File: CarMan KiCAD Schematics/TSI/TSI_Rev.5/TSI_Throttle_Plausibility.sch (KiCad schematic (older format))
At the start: 69 parts, among them Q2 MMBF170, SW1 TS5A3159DBVT, U16 TS372CDT, U18 MCP6004, U22 MCP23016-I_SO, U23 DAC5574IDGS, U3 TS912, U30 TLP293, U6 TS912, U7 MCP6004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

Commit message: Datasheets and notes
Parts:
- SW1: Details (none) -> Analog Switch
- U16: MPN TS372CDT -> (none); OC_FARNELL 1094371 -> (none); PACKAGE 8-SOIC -> (none)
- U22: Field4 Unavailable -> (none); Field5 Microchip -> (none); Field8 None -> (none)
- U23: Details (none) -> 8-bit, Quad, Digital-to-Analog Converter with I2C interface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; Field4 8-bit, Quad, Digital-to-Analog Converter with I2C interface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 -> (none); Field5 None -> (none); Field6 DAC5574IDGS -> (none); Field7 Unavailable -> (none); Field8 Texas Instruments -> (none); Man. (none) -> Texas Instruments
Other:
- note added: "TP \n(J16)"
- note removed: "TP\n(J16)"
- moved on the sheet: C10, C27, C3, C7, D11, D2, D4, R1, R103, R17, R18, R19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

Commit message: General numbering
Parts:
- renumbered RV4 to RV2
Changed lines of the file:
@@
 	5900 2900 5900 2800
 $Comp
-L Device:R_POT_TRIM RV4
+L Device:R_POT_TRIM RV2
 U 1 1 60292796
 P 5900 2200
-F 0 "RV4" H 5830 2246 50  0000 R CNN
+F 0 "RV2" H 5830 2246 50  0000 R CNN
 F 1 "1K" H 5830 2155 50  0000 R CNN
 F 2 "TSI_Rev_2021_Footprint_Lib:Potentiometer" H 5900 2200 50  0001 C CNN

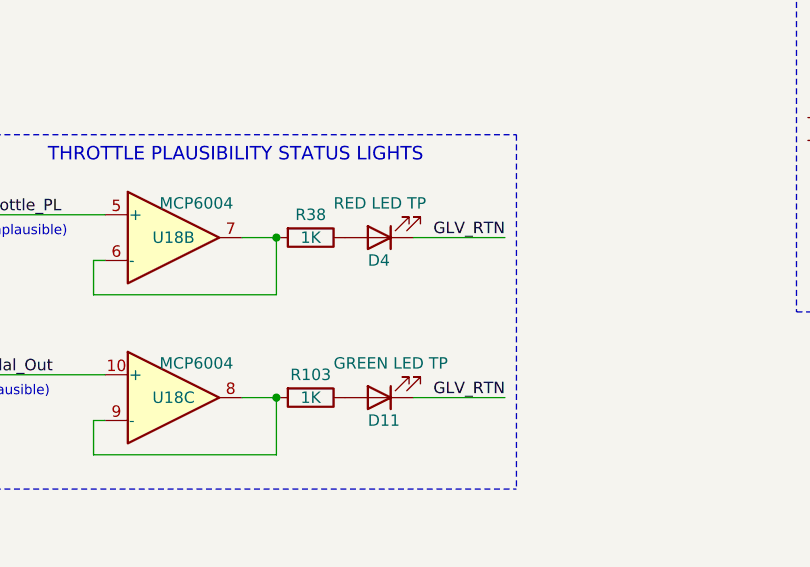
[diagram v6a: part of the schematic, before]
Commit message: Added jumpers across HV-, HV+ & MC+ voltage dividers Comments added to PC Circuit
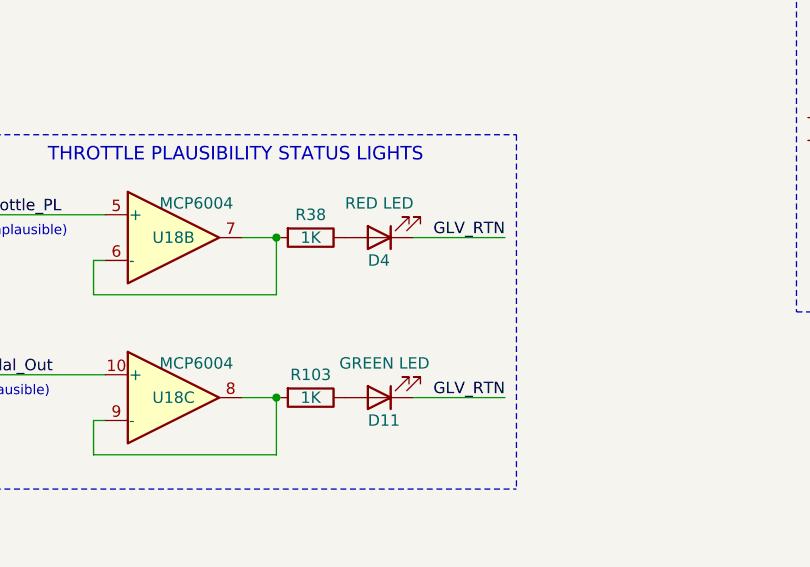
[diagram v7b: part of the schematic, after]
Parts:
- D11: value GREEN LED TP -> GREEN LED
- D4: value RED LED TP -> RED LED
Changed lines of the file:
@@
 AR Path="/5FC85F57/60834B36" Ref="D4"  Part="1"
 F 0 "D4" H 10175 9675 50  0000 R CNN
-F 1 "RED LED TP" H 10325 9425 50  0000 R CNN
+F 1 "RED LED" H 10275 9425 50  0000 R CNN
 F 2 "LED_SMD:LED_0805_2012Metric_Pad1.15x1.40mm_HandSolder" H 10125 9575 50  0001 C CNN
 F 3 "https://www.mouser.com/datasheet/2/678/av02-0112en-ds-hsmx-c1xx-29sep2010-1827222.pdf" H 10125 9575 50  0001 C CNN
@@
 AR Path="/5FC85F57/60823F7C" Ref="D11"  Part="1"
 F 0 "D11" H 10175 10375 50  0000 R CNN
-F 1 "GREEN LED TP" H 10325 10125 50  0000 R CNN
+F 1 "GREEN LED" H 10300 10125 50  0000 R CNN
 F 2 "LED_SMD:LED_0805_2012Metric_Pad1.15x1.40mm_HandSolder" H 10125 10275 50  0001 C CNN
 F 3 "https://www.mouser.com/datasheet/2/678/av02-0112en-ds-hsmx-c1xx-29sep2010-1827222.pdf" H 10125 10275 50  0001 C CNN

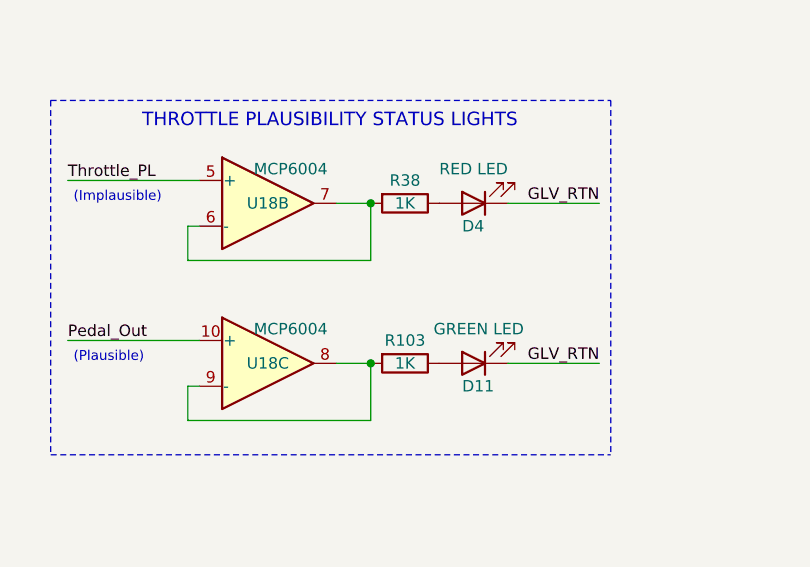
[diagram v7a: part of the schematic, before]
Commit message: Updated Resistor values for LEDs
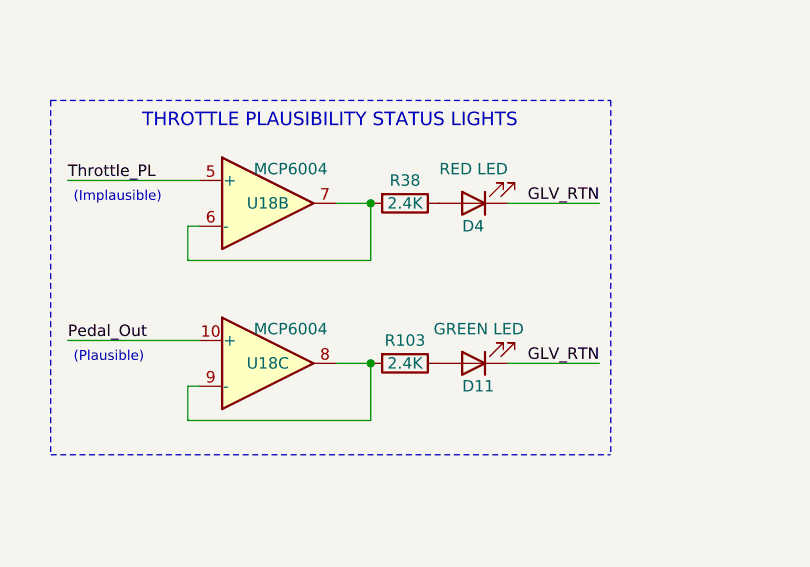
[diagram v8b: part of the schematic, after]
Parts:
- R103, R38: value 1K -> 2.4K
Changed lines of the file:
@@
 P 9825 9575
 F 0 "R38" V 9725 9575 50  0000 C CNN
-F 1 "1K" V 9825 9575 50  0000 C CNN
+F 1 "2.4K" V 9825 9575 50  0000 C CNN
 F 2 "Resistor_SMD:R_0805_2012Metric_Pad1.15x1.40mm_HandSolder" V 9755 9575 50  0001 C CNN
 F 3 "~" H 9825 9575 50  0001 C CNN
@@
 P 9825 10275
 F 0 "R103" V 9725 10275 50  0000 C CNN
-F 1 "1K" V 9825 10275 50  0000 C CNN
+F 1 "2.4K" V 9825 10275 50  0000 C CNN
 F 2 "Resistor_SMD:R_0805_2012Metric_Pad1.15x1.40mm_HandSolder" V 9755 10275 50  0001 C CNN
 F 3 "~" H 9825 10275 50  0001 C CNN
